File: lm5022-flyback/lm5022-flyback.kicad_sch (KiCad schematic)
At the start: 4 parts, among them Q1 EPC2302, U1 LM5022MM

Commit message: lm5022 work
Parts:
- added C1: 1nF, symbol Device:C
- added C2: 100nF, Capacitor_SMD:C_0603_1608Metric, symbol Device:C
- added C3, C4: 100nF, Capacitor_SMD:C_2220_5750Metric, symbol Device:C
- added C5: 1uF, Capacitor_SMD:C_0603_1608Metric, symbol Device:C
- added D1: VS-8EWS12STRL-M3, Package_TO_SOT_SMD:TO-252-2, symbol Device:D_Schottky_AKA
- added J1: CAP, symbol Connector:Screw_Terminal_01x02
- added R3: 100, symbol Device:R
- added R4: 10.8K, symbol Device:R
- added R5: 1, symbol Device:R
- added R6: 10M, symbol Device:R
- added R7: 10K, symbol Device:R
- added R8: 68.1K, symbol Device:R
- added T1: Arthur, symbol transformer:Transformer_1P_1S_Dot
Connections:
- net GND: now also C1.2, C2.2, C3.1, C4.1, C5.2, J1.1 (Pin_1), R5.2, R7.1, R8.2
- net at Q1.2 (S), Q1.4 (S), Q1.6 (S)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: now also R3.2
- net at Q1.3 (D), Q1.5 (D), Q1.7 (D): now also T1.2 (AB)
- net +6V: now reaches U1.1 (VIN)
- net +6V: now also C2.1
- net at U1.4 (VCC): now also C5.1
- net at U1.8 (CS): now also R4.1
- net at U1.9 (RT): now also R8.1
- new net: R5.1, T1.3 (SA)
- new net: C1.1, R3.1, R4.2
- new net: D1.2 (K), T1.4 (SB)
- new net: R6.1, R7.2
- new net +BATT: T1.1 (AA)
- new net -400V: C3.2, C4.2, D1.1 (A), D1.3 (A), J1.2 (Pin_2), R6.2
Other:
- note added: "380uF"

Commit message: add CSA to lm5022
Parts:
- added C6: 100nF, Capacitor_SMD:C_0603_1608Metric, symbol Device:C
- added R10, R11: 1.2K, symbol Device:R
- added R12, R9: 15K, symbol Device:R
- added U2: OP37, symbol op37:OP37
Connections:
- net GND: now also R11.1, R9.1
- net at R5.1, T1.3 (SA): now also R10.1
- net FB: now reaches U1.2 (FB)
- net FB: now also R12.2, U2.6
- new net: R10.2, R9.2, U2.3 (+)
- new net: R11.2, R12.1, U2.2 (-)
- new net +5V: C6.1, U2.7 (V+)
- new net -5V: C6.2, U2.4 (V-)
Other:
- note added: "12.5V/V CSA"

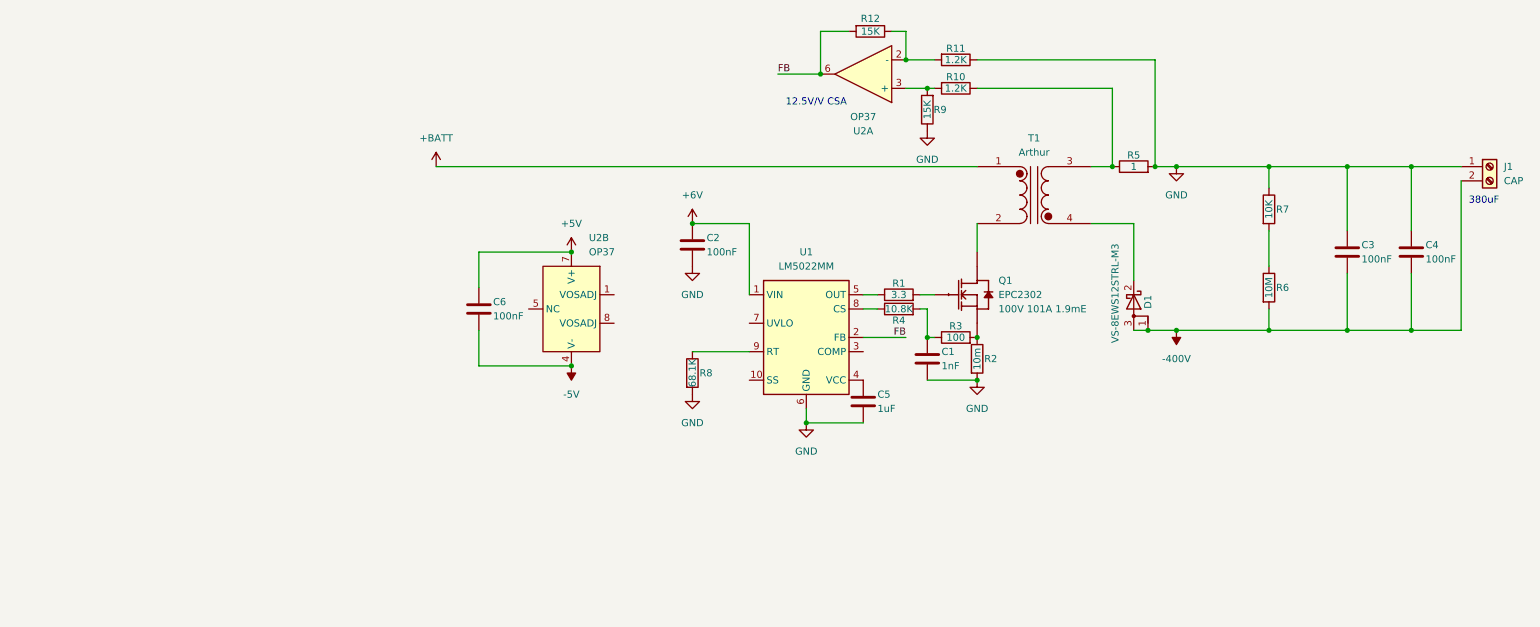
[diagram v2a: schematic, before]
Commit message: progress on flyback
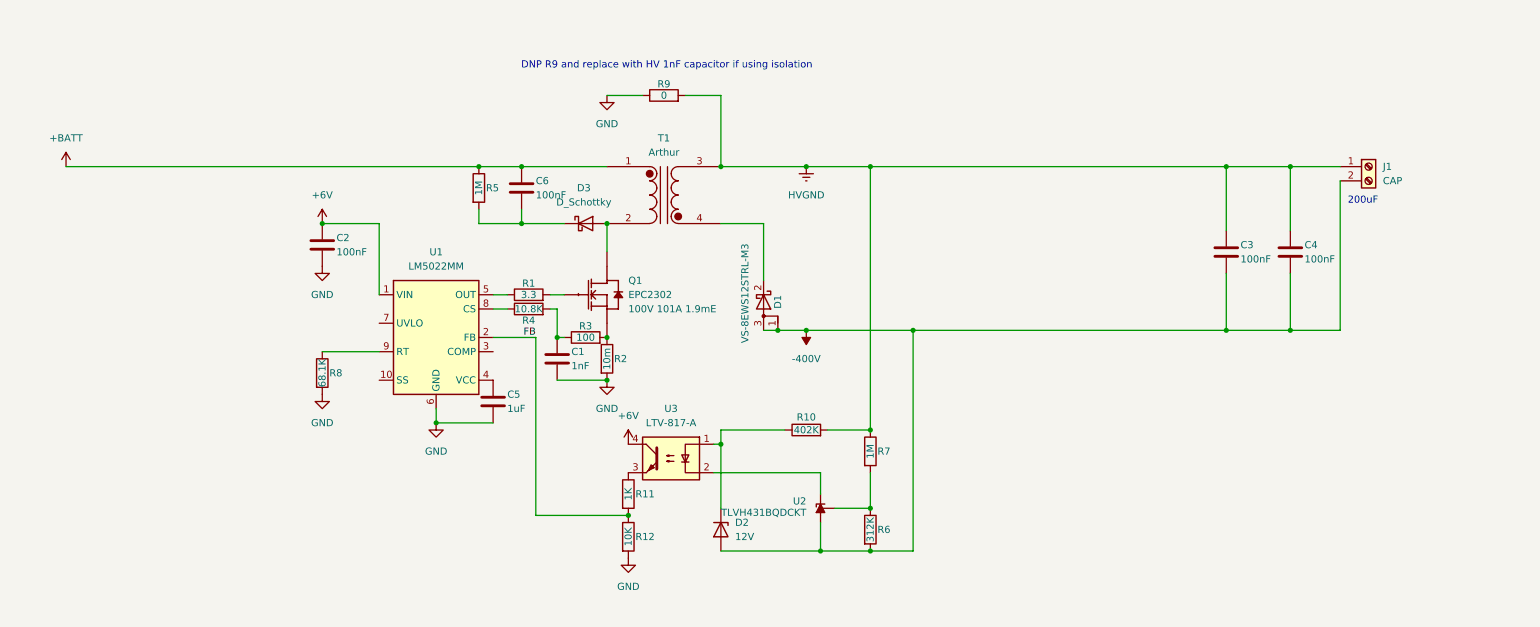
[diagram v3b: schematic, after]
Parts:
- removed U2: OP37, symbol op37:OP37
- added D2: 12V, symbol Device:D_Zener
- added D3: D_Schottky, symbol Device:D_Schottky
- added U2: TLVH431BQDCKT, Package_TO_SOT_SMD:SOT-363_SC-70-6, symbol Reference_Voltage:TL431DCK
- added U3: LTV-817-A, Package_DIP:DIP-4_W7.62mm, symbol Isolator:LTV-817
- C6: footprint Capacitor_SMD:C_0603_1608Metric -> Capacitor_SMD:C_2220_5750Metric
- R10: value 1.2K -> 402K
- R11: value 1.2K -> 1K
- R12: value 15K -> 10K
- R5: value 1 -> 1M
- R6: value 10M -> 312K
- R7: value 10K -> 1M
- R9: value 15K -> 0
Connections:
- net +5V is gone; now on net +BATT: C6.1
- net +6V: now also U3.4
- net +BATT: now also R5.1
- net -400V: now also D2.2 (A), U2.6 (A)
- net FB: now also R11.2, R12.1; no longer R12.2
- net GND: now also R12.2; no longer C3.1, C4.1, J1.1 (Pin_1), R11.1, R5.2, R7.1
- net at Q1.3 (D), Q1.5 (D), Q1.7 (D)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: now also D3.2 (A)
- net HVGND: now reaches R10.2, R9.2
- net HVGND: now also C3.1, C4.1, J1.1 (Pin_1), R7.1, T1.3 (SA)
- net at R6.1, R7.2: now also U2.3 (REF)
- net -5V: no longer names the net of C6.2
- net -5V: now also R5.2, D3.1 (K)
- new net: D2.1 (K), R10.1, U3.1
- new net: U2.1 (K), U3.2
- new net: R11.1, U3.3
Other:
- note added: "200uF"
- note added: "DNP R9 and replace with HV 1nF capacitor if using isolation"
- note removed: "12.5V/V CSA"
- note removed: "380uF"
- moved on the sheet: C1, C2, C3, C4, C5, D1, J1, Q1, R1, R2, R3, R4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

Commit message: update sim and finish high level sch for flyback
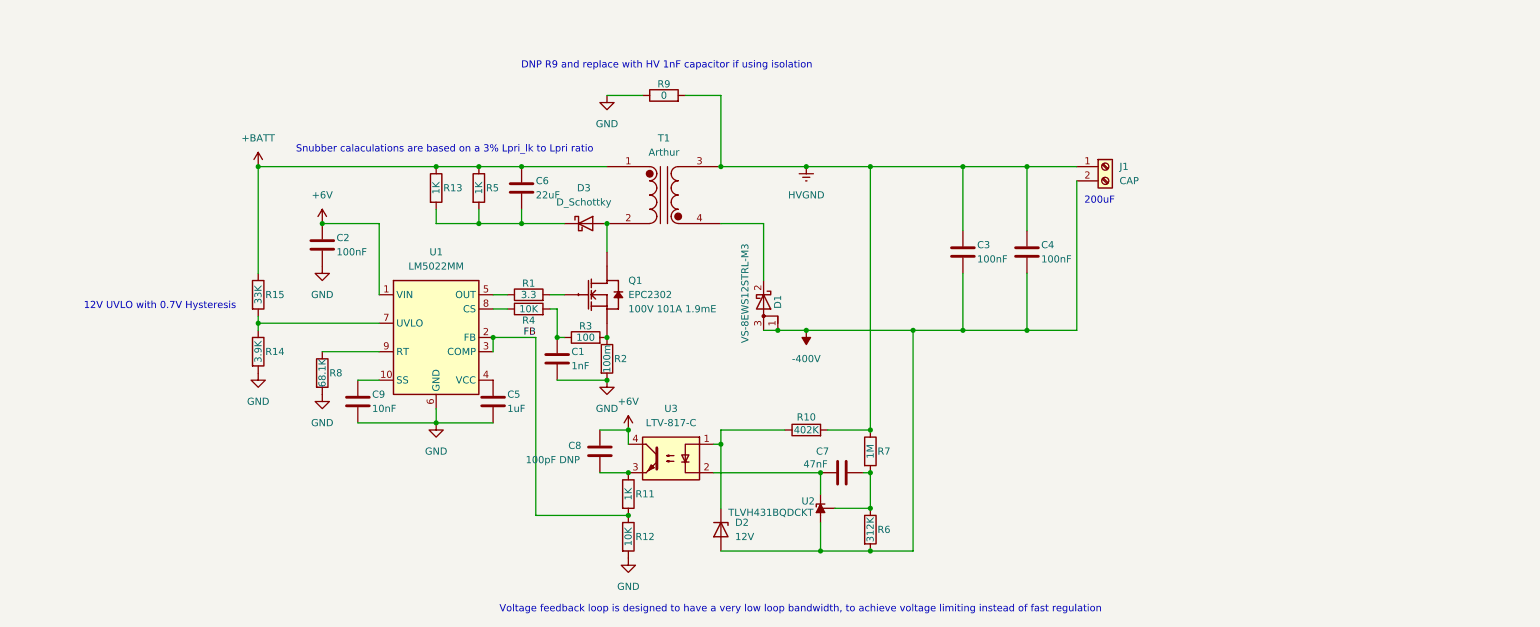
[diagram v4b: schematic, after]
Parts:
- added C7: 47nF, symbol Device:C
- added C8: 100pF DNP, symbol Device:C
- added C9: 10nF, Capacitor_SMD:C_0603_1608Metric, symbol Device:C
- added R13: 1K, symbol Device:R
- added R14: 3.9K, symbol Device:R
- added R15: 33K, symbol Device:R
- C6: value 100nF -> 22uF; footprint Capacitor_SMD:C_2220_5750Metric -> Capacitor_SMD:C_1210_3225Metric
- R2: value 10m -> 100m
- R4: value 10.8K -> 10K
- R5: value 1M -> 1K
- U3: value LTV-817-A -> LTV-817-C
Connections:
- net +6V: now also C8.2
- net +BATT: now also R13.1, R15.1
- net FB: now also U1.3 (COMP)
- net GND: now also C9.2, R14.2
- net at C6.2, D3.1 (K), R5.2: now also R13.2
- net at U2.1 (K), U3.2: now also C7.1
- net at R11.1, U3.3: now also C8.1
- net at U1.10 (SS): now also C9.1
- net at U1.7 (UVLO): now also R14.1, R15.2
- net at R6.1, R7.2, U2.3 (REF): now also C7.2
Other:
- note added: "12V UVLO with 0.7V Hysteresis"
- note added: "Snubber calaculations are based on a 3% Lpri_lk to Lpri ratio"
- note added: "Voltage feedback loop is designed to have a very low loop bandwidth, to achieve voltage limiting instead of fast regulation"
- moved on the sheet: C3, C4, J1

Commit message: footprint assignment for flyback
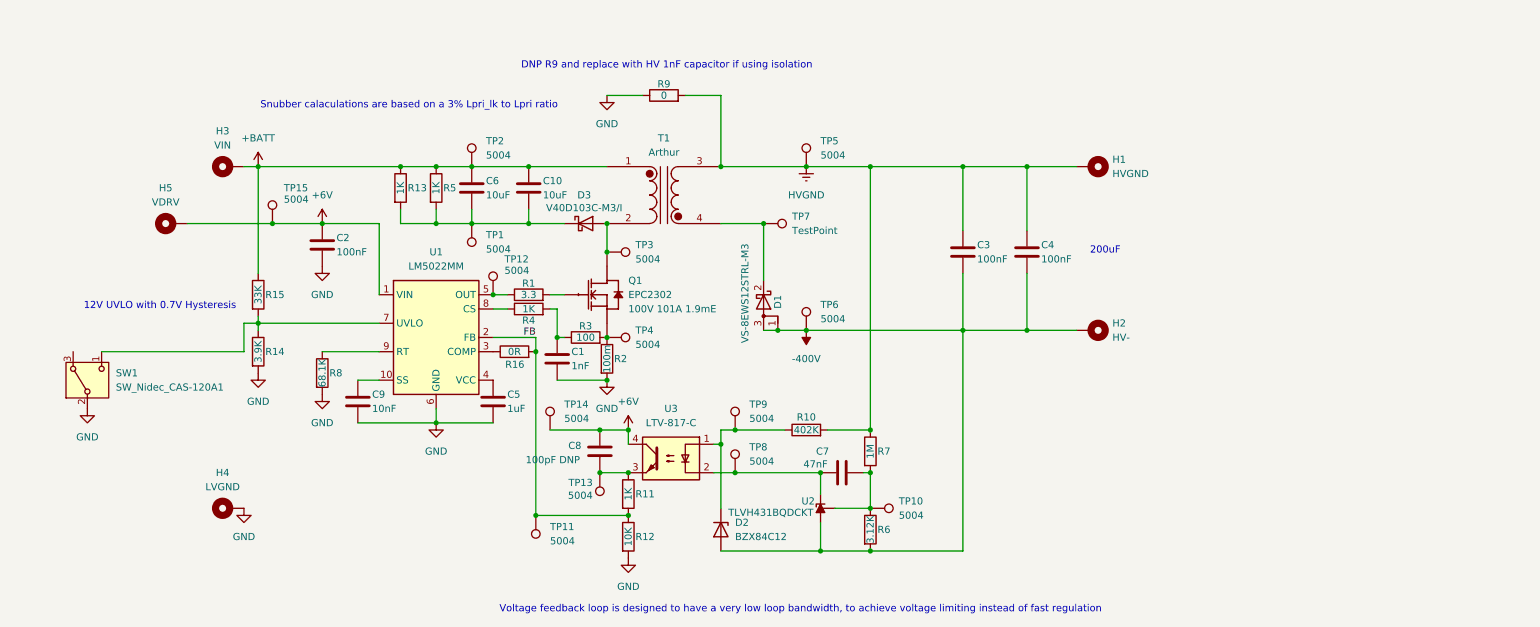
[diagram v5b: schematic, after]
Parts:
- removed D2: 12V, symbol Device:D_Zener
- removed J1: CAP, symbol Connector:Screw_Terminal_01x02
- added C10: 10uF, Capacitor_SMD:C_1210_3225Metric, symbol Device:C
- added D2: BZX84C12, Package_TO_SOT_SMD:SOT-23, symbol Diode:BZX84Cxx
- added H1: HVGND, Pads_Custom:Pad6x4, symbol Mechanical:MountingHole_Pad
- added H2: HV-, Pads_Custom:Pad6x4, symbol Mechanical:MountingHole_Pad
- added H3: VIN, Pads_Custom:Pad6x4, symbol Mechanical:MountingHole_Pad
- added H4: LVGND, Pads_Custom:Pad6x4, symbol Mechanical:MountingHole_Pad
- added H5: VDRV, Pads_Custom:Pad6x4, symbol Mechanical:MountingHole_Pad
- added R16: 0R, Resistor_SMD:R_0603_1608Metric, symbol Device:R
- added SW1: SW_Nidec_CAS-120A1, Button_Switch_SMD:Nidec_Copal_CAS-120A, symbol Switch:SW_Nidec_CAS-120A1
- added TP1, TP10, TP11, TP12, TP13, TP14, TP15, TP2, TP3, TP4, TP5, TP6, TP8, TP9: 5004, TestPoint:TestPoint_Keystone_5000-5004_Miniature, symbol Connector:TestPoint
- added TP7: TestPoint, TestPoint:TestPoint_Keystone_5000-5004_Miniature, symbol Connector:TestPoint
- C1, C7, C8, R15, R3: footprint (none) -> Capacitor_SMD:C_0603_1608Metric
- C6: value 22uF -> 10uF
- D3: value D_Schottky -> V40D103C-M3/I; footprint (none) -> TO_SOT_SMD_Custom:TO-263-2_Diode
- R1: footprint (none) -> Capacitor_SMD:C_0402_1005Metric
- R10, R2, R7: footprint (none) -> Resistor_SMD:R_2512_6332Metric
- R11, R12, R14, R8: footprint (none) -> Resistor_SMD:R_0603_1608Metric
- R13, R5: footprint (none) -> Resistor_SMD:R_0805_2012Metric
- R4: value 10K -> 1K; footprint (none) -> Capacitor_SMD:C_0603_1608Metric
- R6: value 312K -> 3.12K; footprint (none) -> Resistor_SMD:R_0603_1608Metric
- R9: footprint (none) -> Resistor_SMD:R_2010_5025Metric
- T1: footprint (none) -> PlanarTransformer:40-2Transformer
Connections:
- net +6V: now also H5.1, TP14.1, TP15.1
- net +BATT: now also C10.1, H3.1, TP2.1
- net -400V: now also D2.1 (A), H2.1, TP6.1
- net FB: now also R16.2, TP11.1; no longer U1.3 (COMP)
- net GND: now also H4.1, SW1.2 (B)
- net HVGND: now also H1.1, TP5.1
- net at C6.2, D3.1 (K), R13.2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: now also C10.2, TP1.1
- net at R14.1, R15.2, U1.7 (UVLO): now also SW1.1 (C)
- net at Q1.2 (S), Q1.4 (S), Q1.6 (S)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: now also TP4.1
- net at D3.2 (A), Q1.3 (D), Q1.5 (D)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: now also TP3.1
- net at R10.1, U3.1: now also D2.3 (K), TP9.1
- net at C7.1, U2.1 (K), U3.2: now also TP8.1
- net at C8.1, R11.1, U3.3: now also TP13.1
- net at D1.2 (K), T1.4 (SB): now also TP7.1
- net at R1.1, U1.5 (OUT): now also TP12.1
- net at C7.2, R6.1, R7.2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: now also TP10.1
- new net: R16.1, U1.3 (COMP)
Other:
- moved on the sheet: C6, R13, R5
